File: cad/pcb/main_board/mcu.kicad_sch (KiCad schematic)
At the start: 10 parts, among them SW1 SW_DIP_x02, U1 STM32F401R_B-C_Tx, Y1 Crystal_GND23

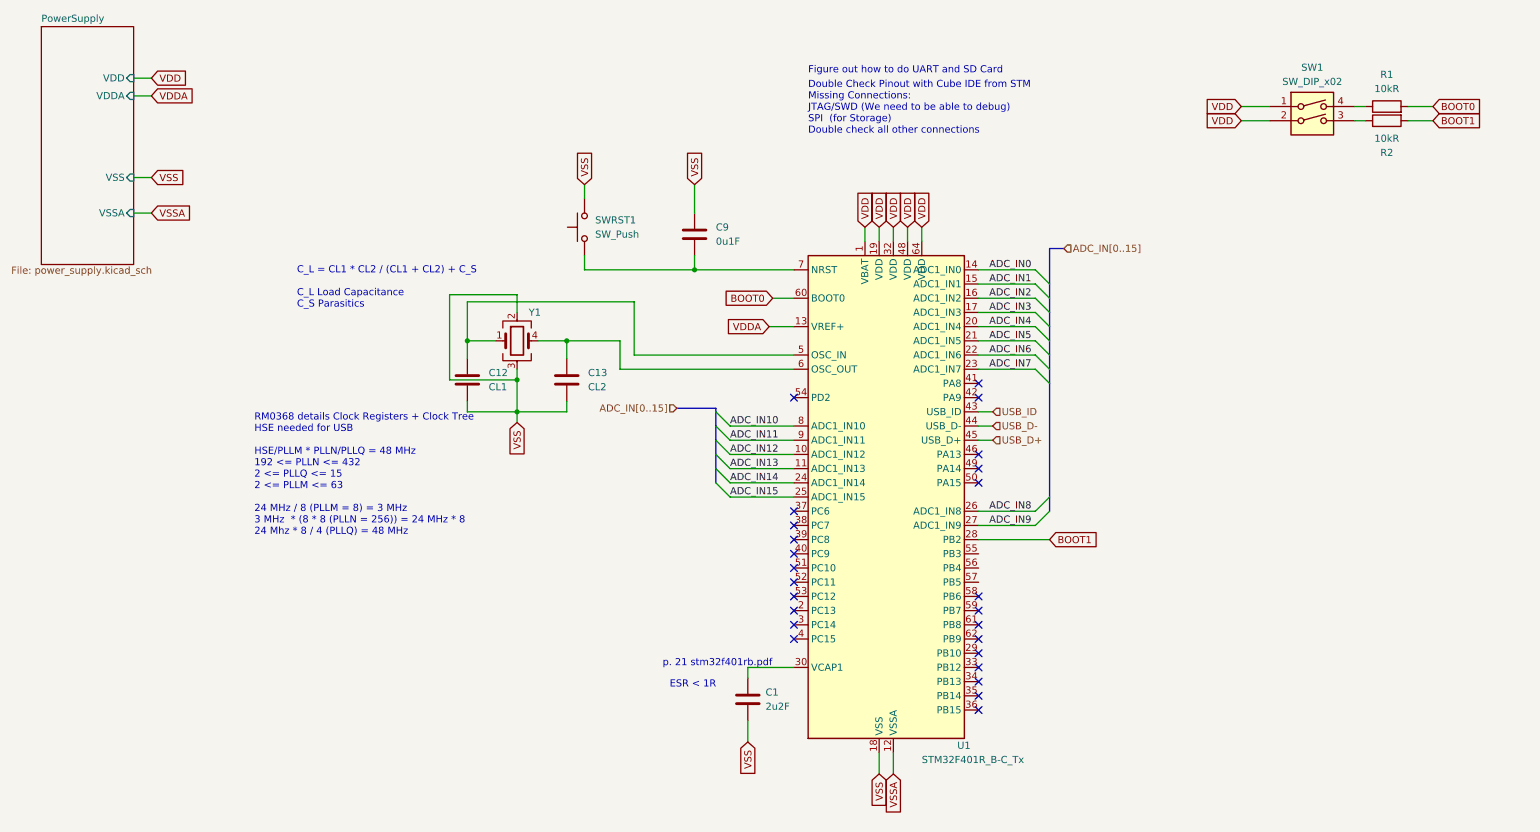
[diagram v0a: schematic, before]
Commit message: Adding JTAG Interface + POGO Pads
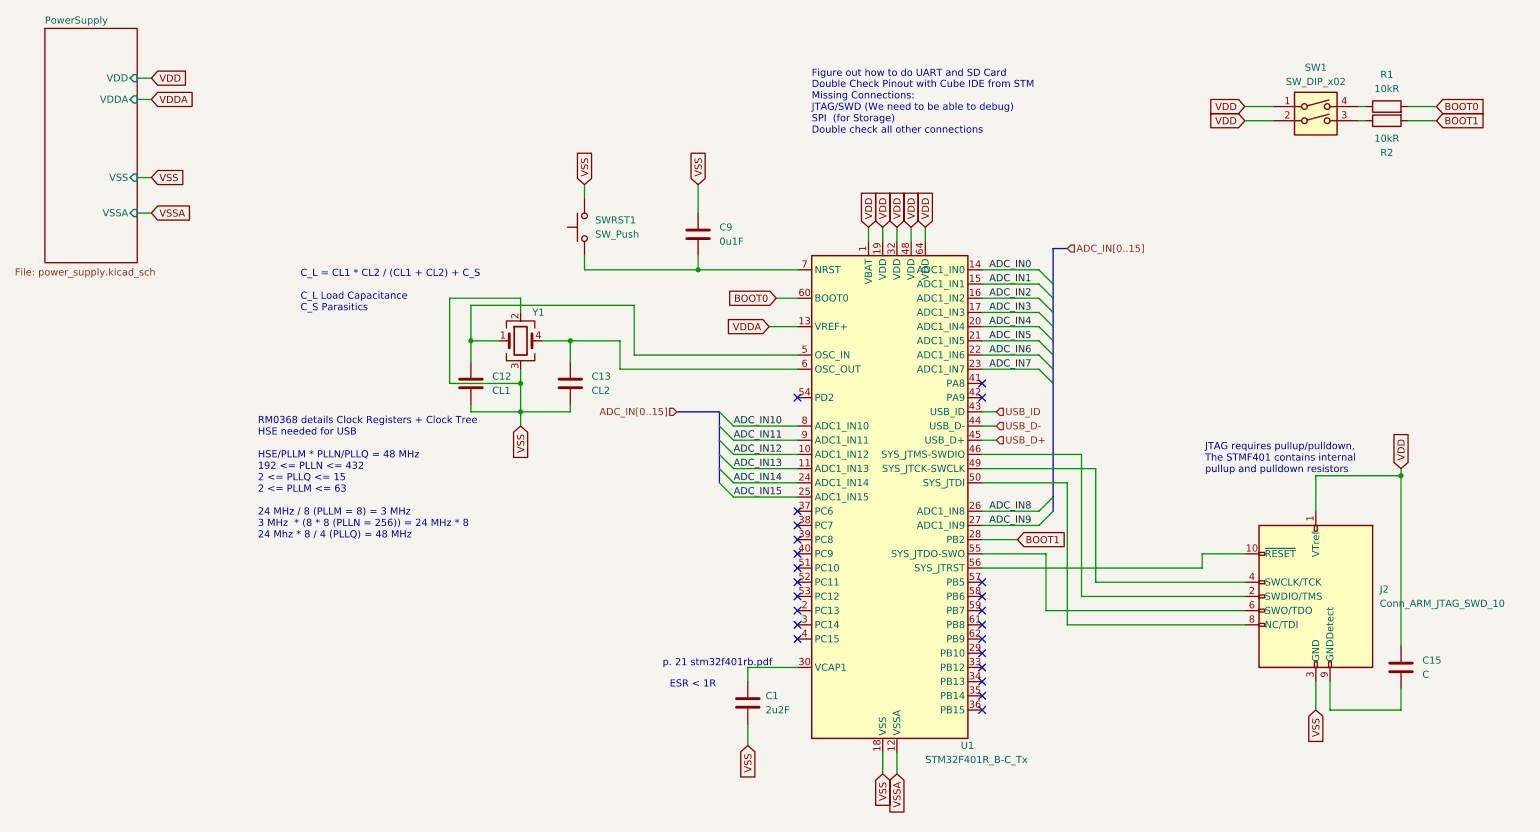
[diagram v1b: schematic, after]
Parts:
- added C15: C, Capacitor_SMD:C_0805_2012Metric, symbol Device:C
- added J2: Conn_ARM_JTAG_SWD_10, local:POGO_JTAG_SWD, symbol Connector:Conn_ARM_JTAG_SWD_10
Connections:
- net VDD: now also C15.1, J2.1 (VTref)
- net VSS: now also J2.3 (GND), J2.5 (GND)
- net at U1.46 (PA13): now also J2.2 (SWDIO/TMS)
- net at U1.49 (PA14): now also J2.4 (SWCLK/TCK)
- net at U1.50 (PA15): now also J2.8 (NC/TDI)
- net at U1.55 (PB3): now also J2.6 (SWO/TDO)
- net at U1.56 (PB4): now also J2.10 (~{RESET})
- new net: C15.2, J2.9 (GNDDetect)
- no-connect marks 25 -> 23
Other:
- note added: "JTAG requires pullup/pulldown, The STMF401 contains internal pullup and pulldown resistors"
- moved on the sheet: C1, C12, C13, C9, SW1, U1, Y1

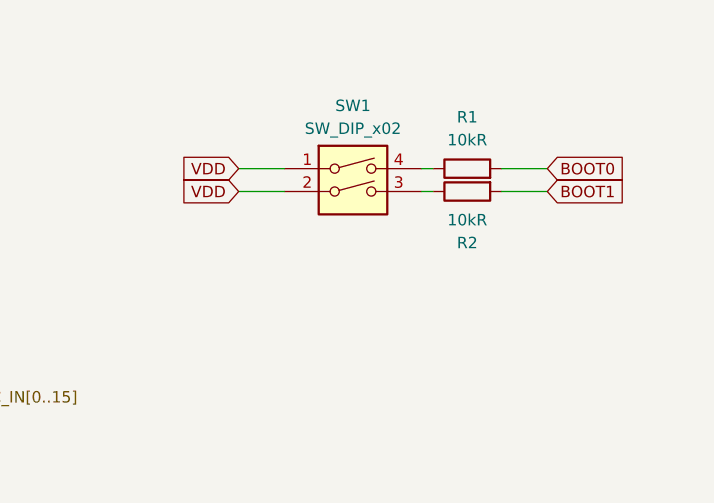
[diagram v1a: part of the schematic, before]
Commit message: More bunching together, some jtag, voltage regulator layout
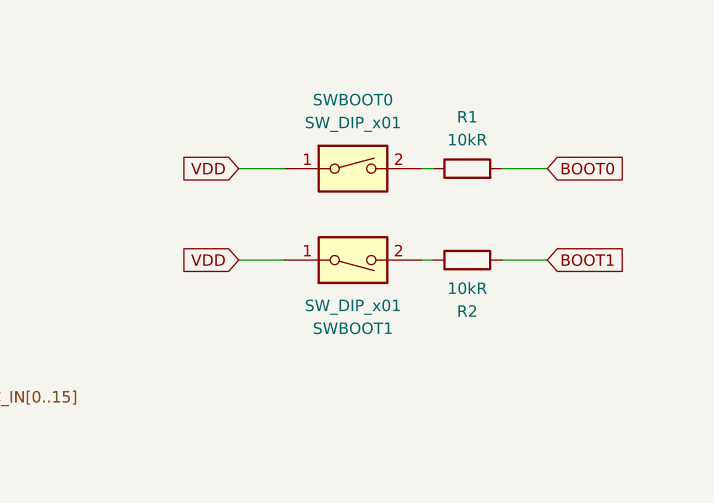
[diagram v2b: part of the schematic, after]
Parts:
- removed SW1: SW_DIP_x02, Button_Switch_SMD:SW_DIP_SPSTx02_Slide_6.7x6.64mm_W6.73mm_P2.54mm_LowProfile_JPin, symbol Switch:SW_DIP_x02
- added SWBOOT0, SWBOOT1: SW_DIP_x01, Button_Switch_SMD:SW_DIP_SPSTx01_Slide_6.7x4.1mm_W6.73mm_P2.54mm_LowProfile_JPin, symbol Switch:SW_DIP_x01
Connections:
- net VDD: now also SWBOOT0.1, SWBOOT1.1
- net at R2.1: now also SWBOOT1.2
- net at R1.1: now also SWBOOT0.2
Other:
- moved on the sheet: R2
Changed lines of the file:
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@@
 	(wire
 		(pts
-			(xy 232.41 33.02) (xy 237.49 33.02)
+			(xy 232.41 40.64) (xy 237.49 40.64)
 		)
 		(stroke
@@
 	(wire
 		(pts
-			(xy 261.62 33.02) (xy 266.7 33.02)
+			(xy 261.62 40.64) (xy 266.7 40.64)
 		)
 		(stroke
@@
 	(wire
 		(pts
-			(xy 252.73 33.02) (xy 254 33.02)
+			(xy 252.73 40.64) (xy 254 40.64)
 		)
 		(stroke
@@
 	(global_label "BOOT1"
 		(shape input)
-		(at 266.7 33.02 0)
+		(at 266.7 40.64 0)
 		(fields_autoplaced yes)
 		(effects
@@
 		)
 		(property "Intersheetrefs" "${INTERSHEET_REFS}"
-			(at 275.7933 33.02 0)
+			(at 275.7933 40.64 0)
 			(effects
 				(font
@@
 	(global_label "VDD"
 		(shape input)
-		(at 232.41 33.02 180)
+		(at 232.41 40.64 180)
 		(fields_autoplaced yes)
 		(effects
@@
 		)
 		(property "Intersheetrefs" "${INTERSHEET_REFS}"
-			(at 225.7962 33.02 0)
+			(at 225.7962 40.64 0)
 			(effects
 				(font
@@
 	(symbol
 		(lib_id "Device:R")
-		(at 257.81 33.02 90)
+		(at 257.81 40.64 90)
 		(mirror x)
 		(unit 1)
@@
 		(dnp no)
 		(property "Reference" "R2"
-			(at 257.81 38.735 90)
+			(at 257.81 46.355 90)
 			(effects
 				(font
@@
 		)
 		(property "Value" "10kR"
-			(at 257.81 36.195 90)
+			(at 257.81 43.815 90)
 			(effects
 				(font
@@
 		)
 		(property "Footprint" "Resistor_SMD:R_0805_2012Metric"
-			(at 257.81 31.242 90)
+			(at 257.81 38.862 90)
 			(effects
 				(font
@@
 		)
 		(property "Datasheet" "~"
-			(at 257.81 33.02 0)
+			(at 257.81 40.64 0)
 			(effects
 				(font
@@
 		)
 		(property "Description" "Resistor"
-			(at 257.81 33.02 0)
+			(at 257.81 40.64 0)
 			(effects
 				(font
@@
 	)
 	(symbol
+		(lib_id "Switch:SW_DIP_x01")
+		(at 245.11 40.64 0)
+		(mirror x)
+		(unit 1)
+		(exclude_from_sim no)
+		(in_bom yes)
+		(on_board yes)
+		(dnp no)
+		(property "Reference" "SWBOOT1"
+			(at 245.11 48.26 0)
+			(effects
+				(font
+					(size 1.27 1.27)
+				)
+			)
+		)
+		(property "Value" "SW_DIP_x01"
+			(at 245.11 45.72 0)
+			(effects
+				(font
+					(size 1.27 1.27)
+				)
+			)
+		)
+		(property "Footprint" "Button_Switch_SMD:SW_DIP_SPSTx01_Slide_6.7x4.1mm_W6.73mm_P2.54mm_LowProfile_JPin"
+			(at 245.11 40.64 0)
+			(effects
+				(font
+					(size 1.27 1.27)
+				)
+				(hide yes)
+			)
+		)
+		(property "Datasheet" "~"
+			(at 245.11 40.64 0)
+			(effects
+				(font
+					(size 1.27 1.27)
+				)
+				(hide yes)
+			)
+		)
+		(property "Description" "1x DIP Switch, Single Pole Single Throw (SPST) switch, small symbol"
+			(at 245.11 40.64 0)
+			(effects
+				(font
+					(size 1.27 1.27)
+				)
+				(hide yes)
+			)
+		)
+		(pin "1"
+		)
+		(pin "2"
+		)
+		(instances
+			(project "main_board"
+				(path "/6c1b8035-64fa-4797-a506-5c9583cb241c/89e1b759-e3da-4961-90e8-6f92bf79e795"
+					(reference "SWBOOT1")
+					(unit 1)
+				)
+			)
+		)
+	)
+	(symbol
 		(lib_id "Switch:SW_Push")
 		(at 114.3 52.07 90)
@@
 				(path "/6c1b8035-64fa-4797-a506-5c9583cb241c/89e1b759-e3da-4961-90e8-6f92bf79e795"
 					(reference "C12")
+					(unit 1)
+				)
+			)
+		)
+	)
+	(symbol
+		(lib_id "Switch:SW_DIP_x01")
+		(at 245.11 30.48 0)
+		(unit 1)
+		(exclude_from_sim no)
+		(in_bom yes)
+		(on_board yes)
+		(dnp no)
+		(fields_autoplaced yes)
+		(property "Reference" "SWBOOT0"
+			(at 245.11 22.86 0)
+			(effects
+				(font
+					(size 1.27 1.27)
+				)
+			)
+		)
+		(property "Value" "SW_DIP_x01"
+			(at 245.11 25.4 0)
+			(effects
+				(font
+					(size 1.27 1.27)
+				)
+			)
+		)
+		(property "Footprint" "Button_Switch_SMD:SW_DIP_SPSTx01_Slide_6.7x4.1mm_W6.73mm_P2.54mm_LowProfile_JPin"
+			(at 245.11 30.48 0)
+			(effects
+				(font
+					(size 1.27 1.27)
+				)
+				(hide yes)
+			)
+		)
+		(property "Datasheet" "~"
+			(at 245.11 30.48 0)
+			(effects
+				(font
+					(size 1.27 1.27)
+				)
+				(hide yes)
+			)
+		)
+		(property "Description" "1x DIP Switch, Single Pole Single Throw (SPST) switch, small symbol"
+			(at 245.11 30.48 0)
+			(effects
+				(font
+					(size 1.27 1.27)
+				)
+				(hide yes)
+			)
+		)
+		(pin "1"
+		)
+		(pin "2"
+		)
+		(instances
+			(project ""
+				(path "/6c1b8035-64fa-4797-a506-5c9583cb241c/89e1b759-e3da-4961-90e8-6f92bf79e795"
+					(reference "SWBOOT0")
 					(unit 1)
 				)
@@
 		)
 	)
-	(symbol
-		(lib_id "Switch:SW_DIP_x02")
-		(at 245.11 33.02 0)
-		(unit 1)
-		(exclude_from_sim no)
-		(in_bom yes)
-		(on_board yes)
-		(dnp no)
-		(fields_autoplaced yes)
-		(property "Reference" "SW1"
-			(at 245.11 23.495 0)
-			(effects
-				(font
-					(size 1.27 1.27)
-				)
-			)
-		)
-		(property "Value" "SW_DIP_x02"
-			(at 245.11 26.035 0)
-			(effects
-				(font
-					(size 1.27 1.27)
-				)
-			)
-		)
-		(property "Footprint" "Button_Switch_SMD:SW_DIP_SPSTx02_Slide_6.7x6.64mm_W6.73mm_P2.54mm_LowProfile_JPin"
-			(at 245.11 33.02 0)
-			(effects
-				(font
-					(size 1.27 1.27)
-				)
-				(hide yes)
-			)
-		)
-		(property "Datasheet" "~"
-			(at 245.11 33.02 0)
-			(effects
-				(font
-					(size 1.27 1.27)
-				)
-				(hide yes)
-			)
-		)
-		(property "Description" "2x DIP Switch, Single Pole Single Throw (SPST) switch, small symbol"
-			(at 245.11 33.02 0)
-			(effects
-				(font
-					(size 1.27 1.27)
-				)
-				(hide yes)
-			)
-		)
-		(pin "1"
-		)
-		(pin "2"
-		)
-		(pin "3"
-		)
-		(pin "4"
+	(sheet
+		(at 17.78 16.51)
+		(size 16.51 41.91)
+		(stroke
+			(width 0.1524)
+			(type solid)
+		)
+		(fill
+			(color 0 0 0 0.0000)
+		)
+		(property "Sheetname" "PowerSupply"
+			(at 17.78 15.7984 0)
+			(effects
+				(font
+					(size 1.27 1.27)
+				)
+				(justify left bottom)
+			)
+		)
+		(property "Sheetfile" "power_supply.kicad_sch"
+			(at 12.3825 59.3725 0)
+			(effects
+				(font
+					(size 1.27 1.27)
+				)
+				(justify left top)
+			)
+		)
+		(pin "VDD" input
+			(at 34.29 25.4 0)
+			(effects
+				(font
+					(size 1.27 1.27)
+				)
+				(justify right)
+			)
+		)
+		(pin "VSS" input
+			(at 34.29 43.18 0)
+			(effects
+				(font
+					(size 1.27 1.27)
+				)
+				(justify right)
+			)
+		)
+		(pin "VSSA" input
+			(at 34.29 49.53 0)
+			(effects
+				(font
+					(size 1.27 1.27)
+				)
+				(justify right)
+			)
+		)
+		(pin "VDDA" input
+			(at 34.29 29.21 0)
+			(effects
+				(font
+					(size 1.27 1.27)
+				)
+				(justify right)
+			)
 		)
 		(instances
 			(project "main_board"
 				(path "/6c1b8035-64fa-4797-a506-5c9583cb241c/89e1b759-e3da-4961-90e8-6f92bf79e795"
-					(reference "SW1")
-					(unit 1)
-				)
-			)
-		)
-	)
-	(sheet
-		(at 17.78 16.51)
-		(size 16.51 41.91)
-		(stroke
-			(width 0.1524)
-			(type solid)
-		)
-		(fill
-			(color 0 0 0 0.0000)
-		)
-		(property "Sheetname" "PowerSupply"
-			(at 17.78 15.7984 0)
-			(effects
-				(font
-					(size 1.27 1.27)
-				)
-				(justify left bottom)
-			)
-		)
-		(property "Sheetfile" "power_supply.kicad_sch"
-			(at 12.3825 59.3725 0)
-			(effects
-				(font
-					(size 1.27 1.27)
-				)
-				(justify left top)
-			)
-		)
-		(pin "VDD" input
-			(at 34.29 25.4 0)
-			(effects
-				(font
-					(size 1.27 1.27)
-				)
-				(justify right)
-			)
-		)
-		(pin "VSS" input
-			(at 34.29 43.18 0)
-			(effects
-				(font
-					(size 1.27 1.27)
-				)
-				(justify right)
-			)
-		)
-		(pin "VSSA" input
-			(at 34.29 49.53 0)
-			(effects
-				(font
-					(size 1.27 1.27)
-				)
-				(justify right)
-			)
-		)
-		(pin "VDDA" input
-			(at 34.29 29.21 0)
-			(effects
-				(font
-					(size 1.27 1.27)
-				)
-				(justify right)
-			)
-		)
-		(instances
-			(project "main_board-rounded"
-				(path "/6c1b8035-64fa-4797-a506-5c9583cb241c/89e1b759-e3da-4961-90e8-6f92bf79e795"
 					(page "3")

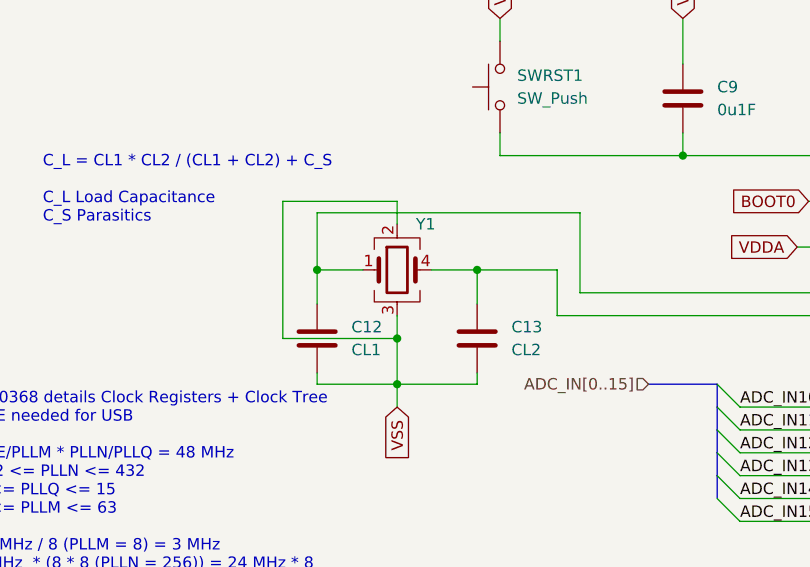
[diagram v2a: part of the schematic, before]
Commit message: Oscillator Selection an and Layouting
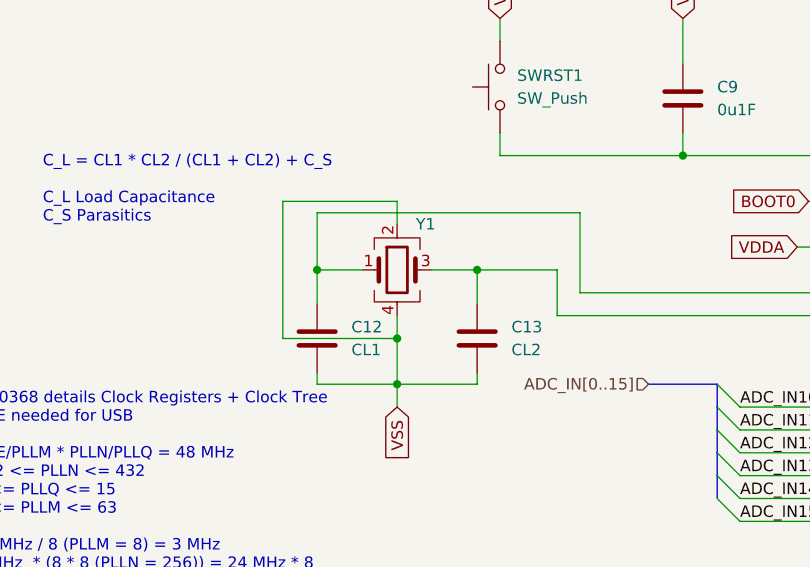
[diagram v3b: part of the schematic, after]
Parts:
- Y1: footprint (none) -> Crystal:Crystal_SMD_2016-4Pin_2.0x1.6mm; symbol Device:Crystal_GND23 -> Device:Crystal_GND24
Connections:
- net VSS: now also Y1.4; no longer Y1.3
- net at C13.1, U1.6 (PH1): now also Y1.3; no longer Y1.4
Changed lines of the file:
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@@
 	)
 	(symbol
-		(lib_id "Device:Crystal_GND23")
+		(lib_id "Device:Crystal_GND24")
 		(at 102.87 72.39 0)
 		(unit 1)
@@
 			)
 		)
-		(property "Footprint" ""
+		(property "Footprint" "Crystal:Crystal_SMD_2016-4Pin_2.0x1.6mm"
 			(at 102.87 72.39 0)
 			(effects
@@
 			)
 		)
-		(property "Description" "Four pin crystal, GND on pins 2 and 3"
+		(property "Description" "Four pin crystal, GND on pins 2 and 4"
 			(at 102.87 72.39 0)
 			(effects
